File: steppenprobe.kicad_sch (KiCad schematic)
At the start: 75 parts, among them J1 USB_C_Receptacle_USB2.0, J2 Conn_01x12, U1 FT2232HL, U11 74LVC1G125, U12 74LVC1G125, U2 XC6206PxxxMR, U3 SRV05-4, U5 74LVC1G125, U7 74LVC1G125, U8 74LVC1G125, U9 74LVC1G125, Y1 Crystal_GND24

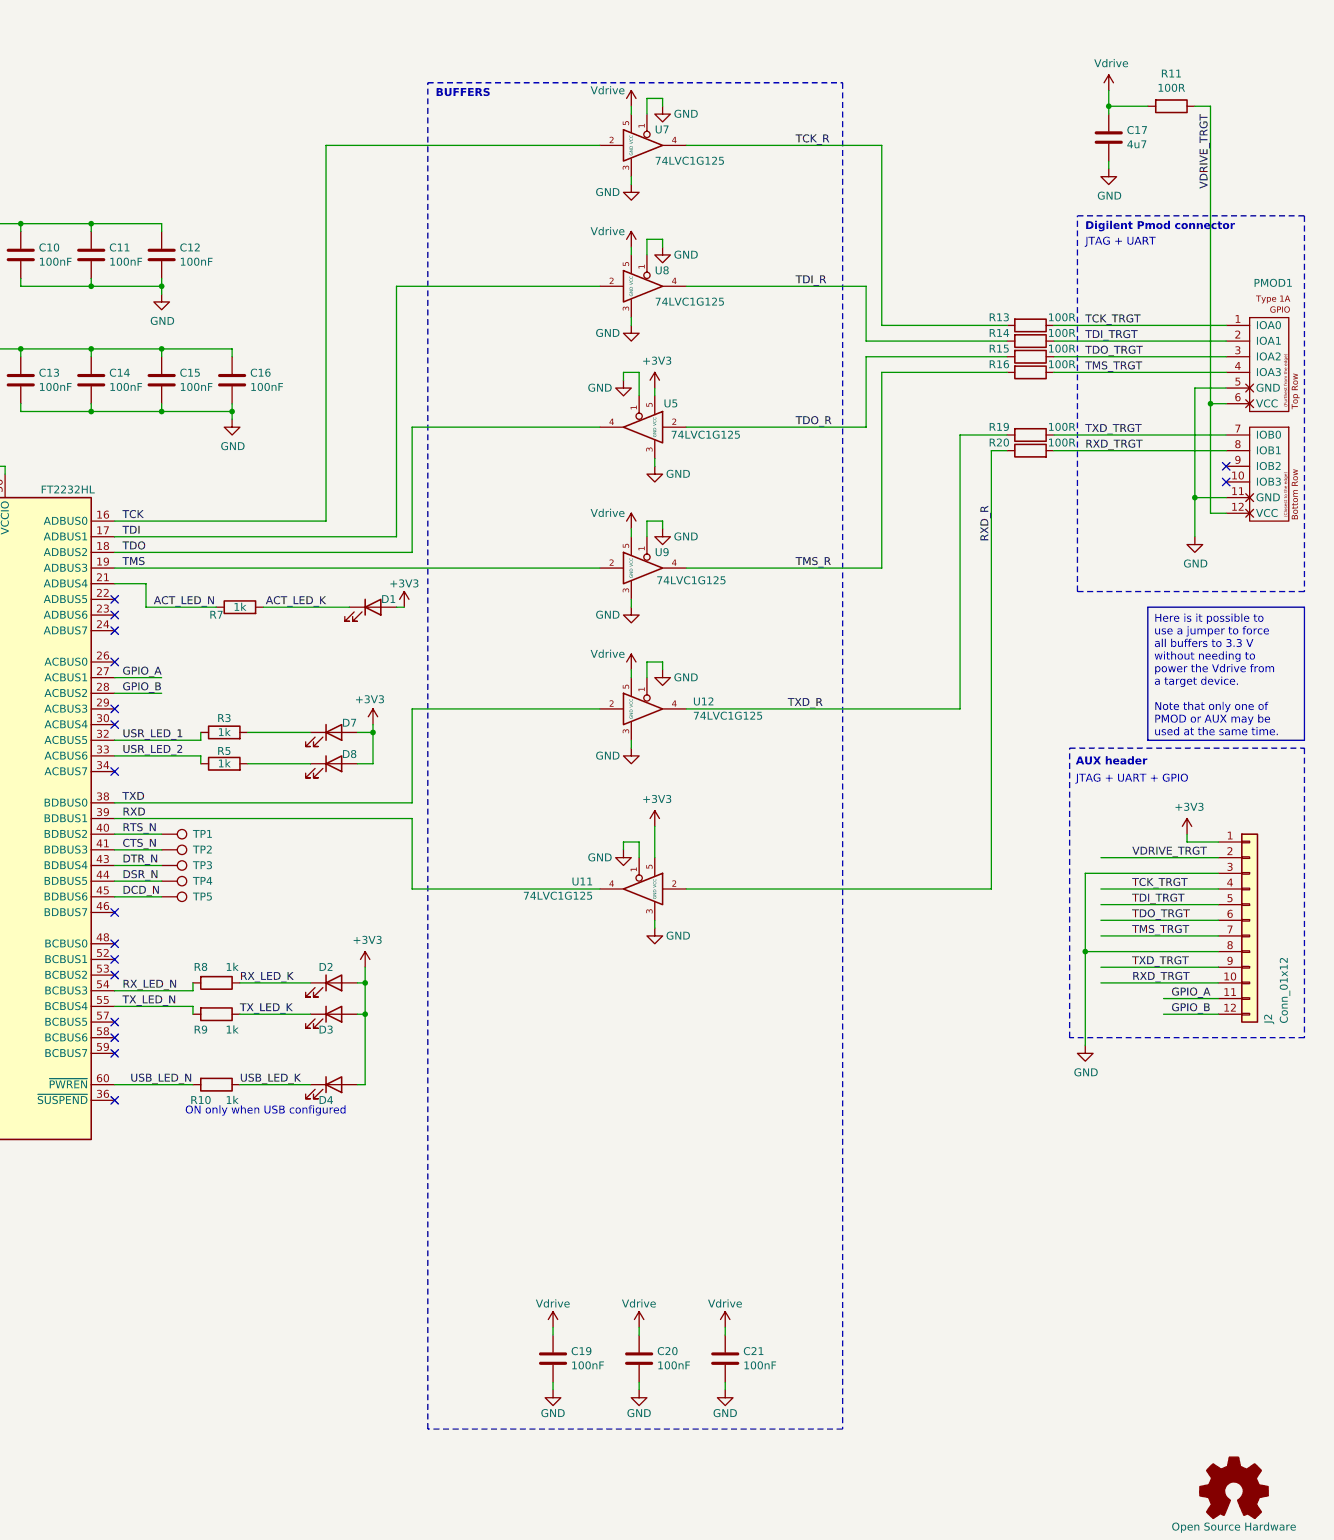
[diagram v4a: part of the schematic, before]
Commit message: Updated footprints, removed testpoints, edited PCB layout.
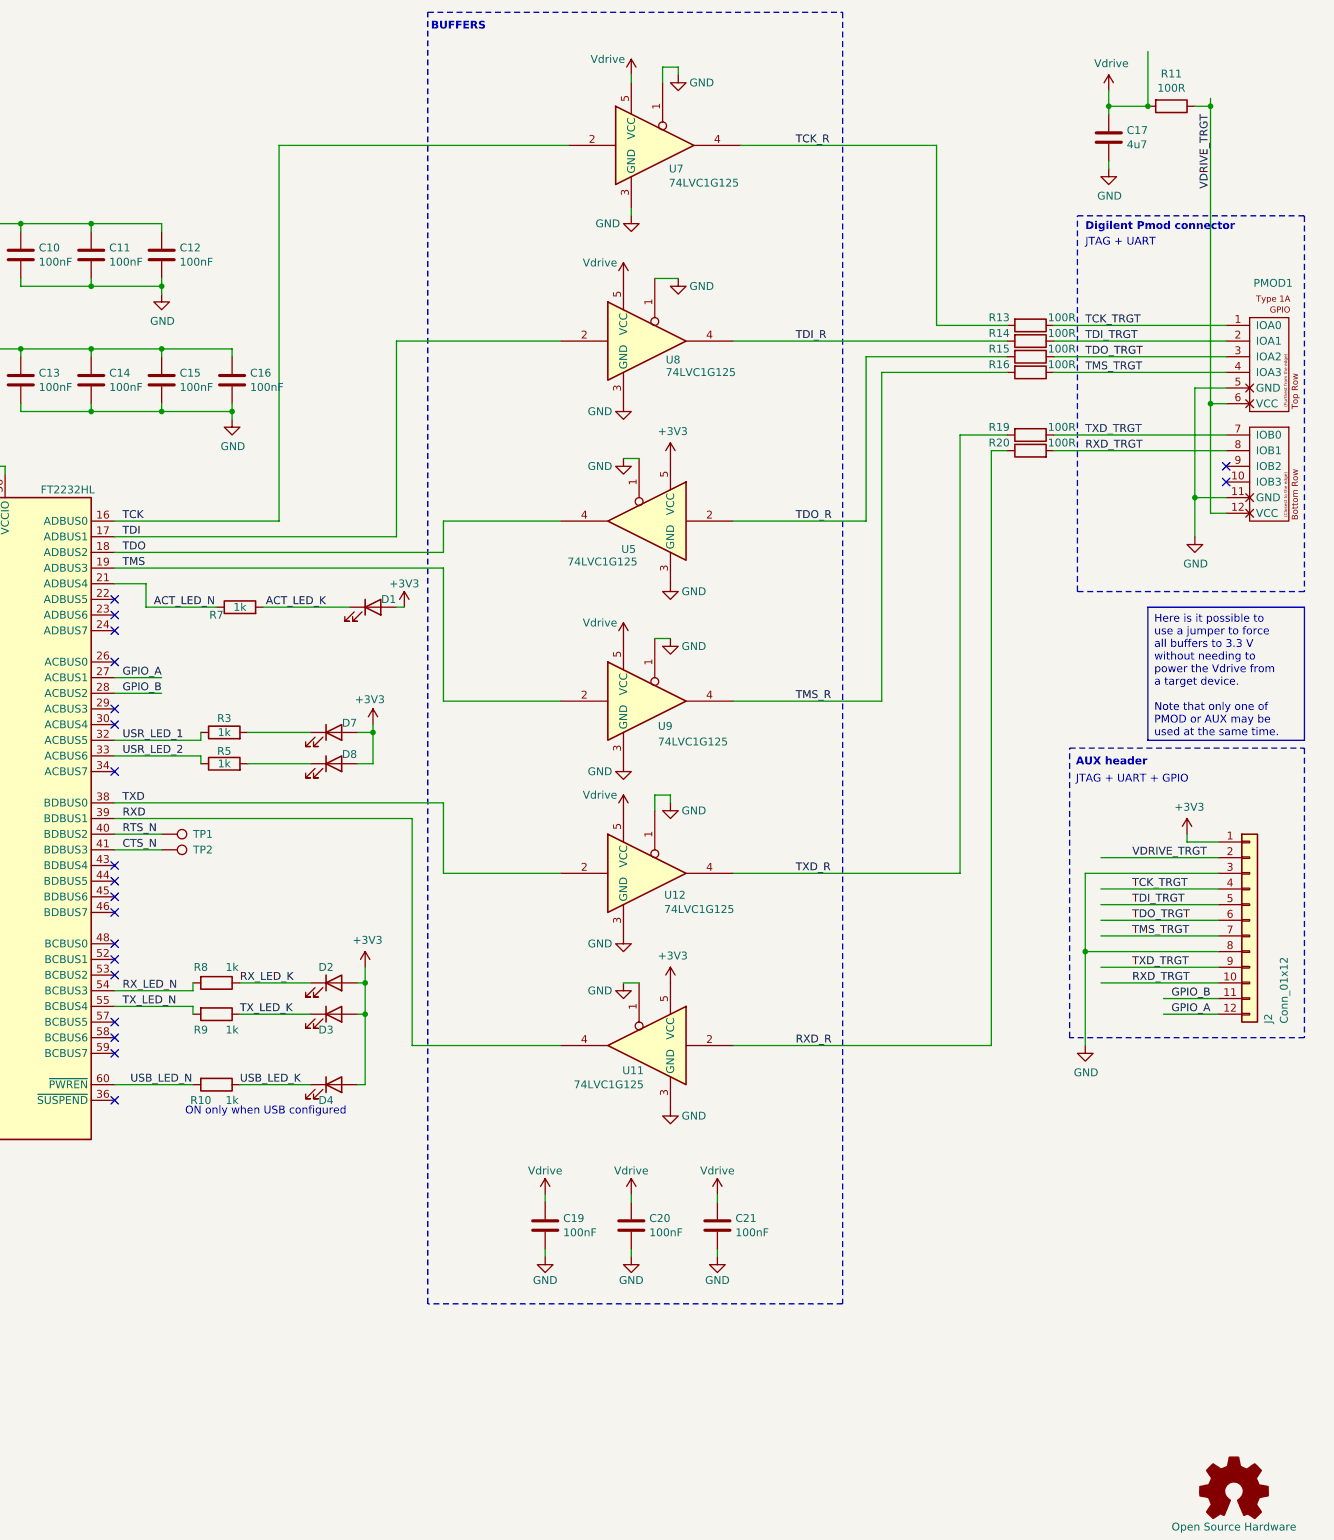
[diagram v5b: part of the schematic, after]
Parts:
- removed TP3, TP4, TP5: TestPoint, TestPoint:TestPoint_Pad_D1.0mm, symbol Connector:TestPoint
- U11, U12, U5, U7, U8, U9: symbol 74xxGxx_power_pins:74LVC1G125-74xGxx -> 74xGxx:74LVC1G125
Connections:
- net GPIO_A: now also J2.12 (Pin_12); no longer J2.11 (Pin_11)
- net GPIO_B: now also J2.11 (Pin_11); no longer J2.12 (Pin_12)
- net DCD_N: no longer names the net of U1.45 (BDBUS6)
- net DSR_N: no longer names the net of U1.44 (BDBUS5)
- net DTR_N: no longer names the net of U1.43 (BDBUS4)
- no-connect marks 20 -> 23
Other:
- moved on the sheet: C19, C20, C21

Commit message: Synced footprints.
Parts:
- C1, C10, C11, C12, C13, C14, C15, C16, C17, C19, C2, C20, C21, C22, C3, C4, C5, C6, C7, C8, C9: footprint Capacitor_SMD:C_0603_1608Metric -> Capacitor_SMD:C_0805_2012Metric
- D1, D2, D3, D4, D5, D7, D8: footprint LED_SMD:LED_0603_1608Metric -> LED_SMD:LED_0805_2012Metric
- FB1, FB2, FB3: footprint Inductor_SMD:L_0603_1608Metric -> Inductor_SMD:L_0805_2012Metric
- R1, R10, R11, R13, R14, R15, R16, R18, R19, R2, R20, R3, R4, R6, R7, R8, R9: footprint Resistor_SMD:R_0603_1608Metric -> Resistor_SMD:R_0805_2012Metric
- R5: footprint Resistor_SMD:R_1206_3216Metric -> Resistor_SMD:R_0805_2012Metric
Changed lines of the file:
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@@
 			)
 		)
-		(property "Footprint" "Resistor_SMD:R_0603_1608Metric"
+		(property "Footprint" "Resistor_SMD:R_0805_2012Metric"
 			(at 138.43 139.192 90)
 			(effects
@@
 			)
 		)
-		(property "Footprint" "Resistor_SMD:R_0603_1608Metric"
+		(property "Footprint" "Resistor_SMD:R_0805_2012Metric"
 			(at 229.87 181.102 90)
 			(effects
@@
 			)
 		)
-		(property "Footprint" "Capacitor_SMD:C_0603_1608Metric"
+		(property "Footprint" "Capacitor_SMD:C_0805_2012Metric"
 			(at 199.0852 63.5 0)
 			(effects
@@
 			)
 		)
-		(property "Footprint" "Inductor_SMD:L_0603_1608Metric"
+		(property "Footprint" "Inductor_SMD:L_0805_2012Metric"
 			(at 138.43 52.832 90)
 			(effects
@@
 			)
 		)
-		(property "Footprint" "Capacitor_SMD:C_0603_1608Metric"
+		(property "Footprint" "Capacitor_SMD:C_0805_2012Metric"
 			(at 143.2052 203.2 0)
 			(effects
@@
 			)
 		)
-		(property "Footprint" "Resistor_SMD:R_0603_1608Metric"
+		(property "Footprint" "Resistor_SMD:R_0805_2012Metric"
 			(at 229.87 192.532 90)
 			(effects
@@
 			)
 		)
-		(property "Footprint" "Resistor_SMD:R_0603_1608Metric"
+		(property "Footprint" "Resistor_SMD:R_0805_2012Metric"
 			(at 361.95 74.422 90)
 			(effects
@@
 			)
 		)
-		(property "Footprint" "Capacitor_SMD:C_0603_1608Metric"
+		(property "Footprint" "Capacitor_SMD:C_0805_2012Metric"
 			(at 134.3152 203.2 0)
 			(effects
@@
 			)
 		)
-		(property "Footprint" "Capacitor_SMD:C_0603_1608Metric"
+		(property "Footprint" "Capacitor_SMD:C_0805_2012Metric"
 			(at 210.5152 83.82 0)
 			(effects
@@
 			)
 		)
-		(property "Footprint" "Resistor_SMD:R_0603_1608Metric"
+		(property "Footprint" "Resistor_SMD:R_0805_2012Metric"
 			(at 384.81 33.782 90)
 			(effects
@@
 			)
 		)
-		(property "Footprint" "Resistor_SMD:R_0603_1608Metric"
+		(property "Footprint" "Resistor_SMD:R_0805_2012Metric"
 			(at 233.68 118.618 90)
 			(effects
@@
 			)
 		)
-		(property "Footprint" "Capacitor_SMD:C_0603_1608Metric"
+		(property "Footprint" "Capacitor_SMD:C_0805_2012Metric"
 			(at 210.5152 63.5 0)
 			(effects
@@
 			)
 		)
-		(property "Footprint" "Inductor_SMD:L_0603_1608Metric"
+		(property "Footprint" "Inductor_SMD:L_0805_2012Metric"
 			(at 138.43 73.152 90)
 			(effects
@@
 			)
 		)
-		(property "Footprint" "Resistor_SMD:R_0603_1608Metric"
+		(property "Footprint" "Resistor_SMD:R_0805_2012Metric"
 			(at 61.722 137.16 90)
 			(effects
@@
 			)
 		)
-		(property "Footprint" "Capacitor_SMD:C_0603_1608Metric"
+		(property "Footprint" "Capacitor_SMD:C_0805_2012Metric"
 			(at 221.9452 83.82 0)
 			(effects
@@
 			)
 		)
-		(property "Footprint" "Resistor_SMD:R_0603_1608Metric"
+		(property "Footprint" "Resistor_SMD:R_0805_2012Metric"
 			(at 361.95 87.122 90)
 			(effects
@@
 			)
 		)
-		(property "Footprint" "Capacitor_SMD:C_0603_1608Metric"
+		(property "Footprint" "Capacitor_SMD:C_0805_2012Metric"
 			(at 65.7352 90.17 0)
 			(effects
@@
 			)
 		)
-		(property "Footprint" "Capacitor_SMD:C_0603_1608Metric"
+		(property "Footprint" "Capacitor_SMD:C_0805_2012Metric"
 			(at 148.2852 63.5 0)
 			(effects
@@
 			)
 		)
-		(property "Footprint" "LED_SMD:LED_0603_1608Metric"
+		(property "Footprint" "LED_SMD:LED_0805_2012Metric"
 			(at 118.11 91.44 0)
 			(effects
@@
 			)
 		)
-		(property "Footprint" "Resistor_SMD:R_0603_1608Metric"
+		(property "Footprint" "Resistor_SMD:R_0805_2012Metric"
 			(at 118.872 143.51 90)
 			(effects
@@
 			)
 		)
-		(property "Footprint" "Capacitor_SMD:C_0603_1608Metric"
+		(property "Footprint" "Capacitor_SMD:C_0805_2012Metric"
 			(at 199.0852 83.82 0)
 			(effects
@@
 			)
 		)
-		(property "Footprint" "Capacitor_SMD:C_0603_1608Metric"
+		(property "Footprint" "Capacitor_SMD:C_0805_2012Metric"
 			(at 135.5852 116.84 0)
 			(effects
@@
 			)
 		)
-		(property "Footprint" "Resistor_SMD:R_0603_1608Metric"
+		(property "Footprint" "Resistor_SMD:R_0805_2012Metric"
 			(at 361.95 76.962 90)
 			(effects
@@
 			)
 		)
-		(property "Footprint" "Capacitor_SMD:C_0603_1608Metric"
+		(property "Footprint" "Capacitor_SMD:C_0805_2012Metric"
 			(at 312.1152 220.98 0)
 			(effects
@@
 			)
 		)
-		(property "Footprint" "LED_SMD:LED_0603_1608Metric"
+		(property "Footprint" "LED_SMD:LED_0805_2012Metric"
 			(at 248.92 194.31 0)
 			(effects
@@
 			)
 		)
-		(property "Footprint" "LED_SMD:LED_0603_1608Metric"
+		(property "Footprint" "LED_SMD:LED_0805_2012Metric"
 			(at 248.92 142.24 0)
 			(effects
@@
 			)
 		)
-		(property "Footprint" "Resistor_SMD:R_0603_1608Metric"
+		(property "Footprint" "Resistor_SMD:R_0805_2012Metric"
 			(at 361.95 69.342 90)
 			(effects
@@
 			)
 		)
-		(property "Footprint" "Capacitor_SMD:C_0603_1608Metric"
+		(property "Footprint" "Capacitor_SMD:C_0805_2012Metric"
 			(at 159.7152 83.82 0)
 			(effects
@@
 			)
 		)
-		(property "Footprint" "Capacitor_SMD:C_0603_1608Metric"
+		(property "Footprint" "Capacitor_SMD:C_0805_2012Metric"
 			(at 148.2852 116.84 0)
 			(effects
@@
 			)
 		)
-		(property "Footprint" "Capacitor_SMD:C_0603_1608Metric"
+		(property "Footprint" "Capacitor_SMD:C_0805_2012Metric"
 			(at 221.9452 63.5 0)
 			(effects
@@
 			)
 		)
-		(property "Footprint" "Resistor_SMD:R_0603_1608Metric"
+		(property "Footprint" "Resistor_SMD:R_0805_2012Metric"
 			(at 361.95 93.218 90)
 			(effects
@@
 			)
 		)
-		(property "Footprint" "Resistor_SMD:R_1206_3216Metric"
+		(property "Footprint" "Resistor_SMD:R_0805_2012Metric"
 			(at 231.14 144.018 90)
 			(effects
@@
 			)
 		)
-		(property "Footprint" "Resistor_SMD:R_0603_1608Metric"
+		(property "Footprint" "Resistor_SMD:R_0805_2012Metric"
 			(at 116.332 82.55 90)
 			(effects
@@
 			)
 		)
-		(property "Footprint" "Resistor_SMD:R_0603_1608Metric"
+		(property "Footprint" "Resistor_SMD:R_0805_2012Metric"
 			(at 231.14 138.938 90)
 			(effects
@@
 			)
 		)
-		(property "Footprint" "Capacitor_SMD:C_0603_1608Metric"
+		(property "Footprint" "Capacitor_SMD:C_0805_2012Metric"
 			(at 284.1752 220.98 0)
 			(effects
@@
 			)
 		)
-		(property "Footprint" "Capacitor_SMD:C_0603_1608Metric"
+		(property "Footprint" "Capacitor_SMD:C_0805_2012Metric"
 			(at 233.3752 83.82 0)
 			(effects
@@
 			)
 		)
-		(property "Footprint" "Resistor_SMD:R_0603_1608Metric"
+		(property "Footprint" "Resistor_SMD:R_0805_2012Metric"
 			(at 229.87 176.022 90)
 			(effects
@@
 			)
 		)
-		(property "Footprint" "Capacitor_SMD:C_0603_1608Metric"
+		(property "Footprint" "Capacitor_SMD:C_0805_2012Metric"
 			(at 100.0252 90.17 0)
 			(effects
@@
 			)
 		)
-		(property "Footprint" "LED_SMD:LED_0603_1608Metric"
+		(property "Footprint" "LED_SMD:LED_0805_2012Metric"
 			(at 248.92 182.88 0)
 			(effects
@@
 			)
 		)
-		(property "Footprint" "LED_SMD:LED_0603_1608Metric"
+		(property "Footprint" "LED_SMD:LED_0805_2012Metric"
 			(at 248.92 177.8 0)
 			(effects
@@
 			)
 		)
-		(property "Footprint" "Resistor_SMD:R_0603_1608Metric"
+		(property "Footprint" "Resistor_SMD:R_0805_2012Metric"
 			(at 361.95 71.882 90)
 			(effects
@@
 			)
 		)
-		(property "Footprint" "Capacitor_SMD:C_0603_1608Metric"
+		(property "Footprint" "Capacitor_SMD:C_0805_2012Metric"
 			(at 298.1452 220.98 0)
 			(effects
@@
 			)
 		)
-		(property "Footprint" "Capacitor_SMD:C_0603_1608Metric"
+		(property "Footprint" "Capacitor_SMD:C_0805_2012Metric"
 			(at 148.2852 83.82 0)
 			(effects
@@
 			)
 		)
-		(property "Footprint" "Capacitor_SMD:C_0603_1608Metric"
+		(property "Footprint" "Capacitor_SMD:C_0805_2012Metric"
 			(at 159.7152 63.5 0)
 			(effects
@@
 			)
 		)
-		(property "Footprint" "Inductor_SMD:L_0603_1608Metric"
+		(property "Footprint" "Inductor_SMD:L_0805_2012Metric"
 			(at 58.42 76.962 90)
 			(effects
@@
 			)
 		)
-		(property "Footprint" "Capacitor_SMD:C_0603_1608Metric"
+		(property "Footprint" "Capacitor_SMD:C_0805_2012Metric"
 			(at 375.6152 44.45 0)
 			(effects
@@
 			)
 		)
-		(property "Footprint" "Resistor_SMD:R_0603_1608Metric"
+		(property "Footprint" "Resistor_SMD:R_0805_2012Metric"
 			(at 55.372 137.16 90)
 			(effects
@@
 			)
 		)
-		(property "Footprint" "LED_SMD:LED_0603_1608Metric"
+		(property "Footprint" "LED_SMD:LED_0805_2012Metric"
 			(at 255.27 116.84 0)
 			(effects
@@
 			)
 		)
-		(property "Footprint" "LED_SMD:LED_0603_1608Metric"
+		(property "Footprint" "LED_SMD:LED_0805_2012Metric"
 			(at 248.92 137.16 0)
 			(effects

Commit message: Fixed part numbering.
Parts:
- renumbered C9 to C10, C10 to C11, C13 to C12, C11 to C13, C12 to C15, C15 to C16, C16 to C17, C19 to C18, C20 to C19, C21 to C20, C17 to C21, C22 to C4, C4 to C5, C5 to C6, C6 to C7, C7 to C8, C8 to C9, D5 to D1, D7 to D2, D8 to D3, D2 to D4, D3 to D5, D4 to D6, D1 to D7, R5 to R10, R7 to R11, R13 to R12, R14 to R13, R15 to R14, R16 to R15, R19 to R16, R20 to R17, R11 to R18, R18 to R3, R6 to R5, R8 to R6, R9 to R7, R10 to R8, R3 to R9, U3 to U1, U1 to U3, U5 to U4, U11 to U5, U8 to U6, U9 to U7, U12 to U8, U7 to U9

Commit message: Updated part numbers.
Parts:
- C1, C2, C21, C6, C7, C8: LCSC_PN C19666 -> (none); MPN CL10A475KO8NNNC -> CL21A475KPFNNNG; MPN2 EMK107ABJ475KA-T -> (none); Manufacturer2 Taiyo Yuden -> (none)
- C10, C11, C12, C13, C14, C15, C16, C17, C18, C19, C20, C4, C9: LCSC_PN C14663 -> (none); MPN CC0603KRX7R9BB104 -> CL21B104KACNNND; MPN2 CL10B104KB8NNNC -> (none); Manufacturer Yageo -> Murata Electronics; Manufacturer2 Samsung Electro-Mechanics -> (none)
- C3, C5: LCSC_PN C1656 -> (none); MPN C0603C270J5GAC -> CL21C270JCANNNC; MPN2 CL10C270JB8NNNC -> (none); Manufacturer Kemet -> Murata Electronics; Manufacturer2 Samsung Electro-Mechanics -> (none)
- D1, D6: value LED -> Green LED; LCSC_PN C72043 -> (none); MPN 19-217/GHC-YR1S2/3T -> 150080GS75000; MPN2 150060GS75000 -> (none); Manufacturer Everlight Elec -> Wurth Electronic; Manufacturer2 Wurth Electronic -> (none)
- D2, D3: value LED -> White LED; MPN (none) -> IN-S85AT5UW; Manufacturer (none) -> Inolux
- D4, D5: value LED -> Amber LED; LCSC_PN C72043 -> (none); MPN 19-217/GHC-YR1S2/3T -> 150080AS75000; MPN2 150060GS75000 -> (none); Manufacturer Everlight Elec -> Wurth Electronic; Manufacturer2 Wurth Electronic -> (none)
- D7: value LED -> Blue LED; LCSC_PN C72043 -> (none); MPN 19-217/GHC-YR1S2/3T -> 150080BS75000; MPN2 150060GS75000 -> (none); Manufacturer Everlight Elec -> Wurth Electronic; Manufacturer2 Wurth Electronic -> (none)
- FB1, FB2, FB3: LCSC_PN C85831 -> (none); MPN BLM18KG121TN1D -> BLM21PG121SZ1D; MPN2 BKP1608HS121-T -> (none); Manufacturer2 Taiyo Yuden -> (none)
- LOGO1: now not fitted
- R1, R2: LCSC_PN C23186 -> (none)
- R11, R3, R6, R7, R8: LCSC_PN C21190 -> (none)
- R12, R13, R14, R15, R16, R17, R18: LCSC_PN C22775 -> (none)
- R4: LCSC_PN C22790 -> (none)
- R5: LCSC_PN C25804 -> (none)
- U1: LCSC_PN C85364 -> (none)
- U2: LCSC_PN C5446 -> (none); MPN XC6206P332MR -> XC6206P332MR-G
- U3: LCSC_PN C27882 -> (none)
- U4, U5, U6, U7, U8, U9: LCSC_PN C12519 -> (none)
- Y1: LCSC_PN C9002 -> (none)
